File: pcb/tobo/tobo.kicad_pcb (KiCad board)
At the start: 2 copper layers, 57.5 x 61 mm, 87 parts, among them J2 Conn_01x02_Pin, J4 Molex 538-54548-2472, J5 Conn_01x09_Pin, J6 Conn_01x09_Pin, J7 Conn_01x09_Pin, J8 Hroparts Elec TYPE-C-31-M-12, U1 TS5A23167, U10 5015, U11 5015, U12 5015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

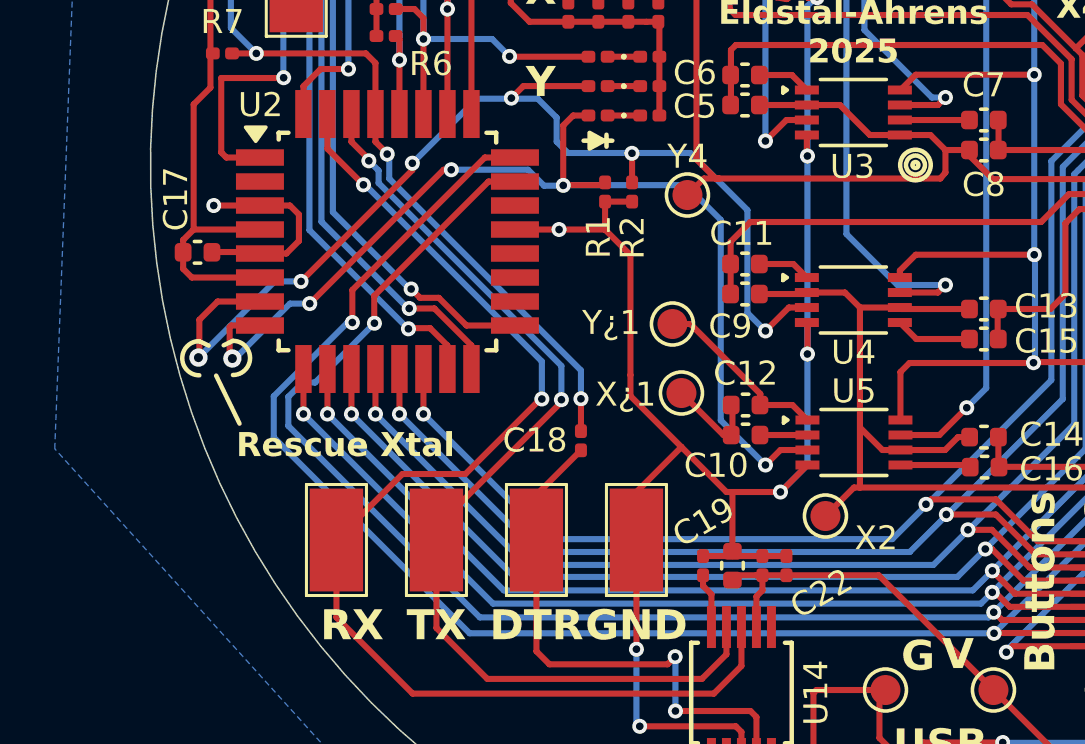
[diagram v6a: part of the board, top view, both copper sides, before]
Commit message: Solution to the PCB error in v0.3a
If you've got a v0.4 board, no need to futz around with RX/TX.
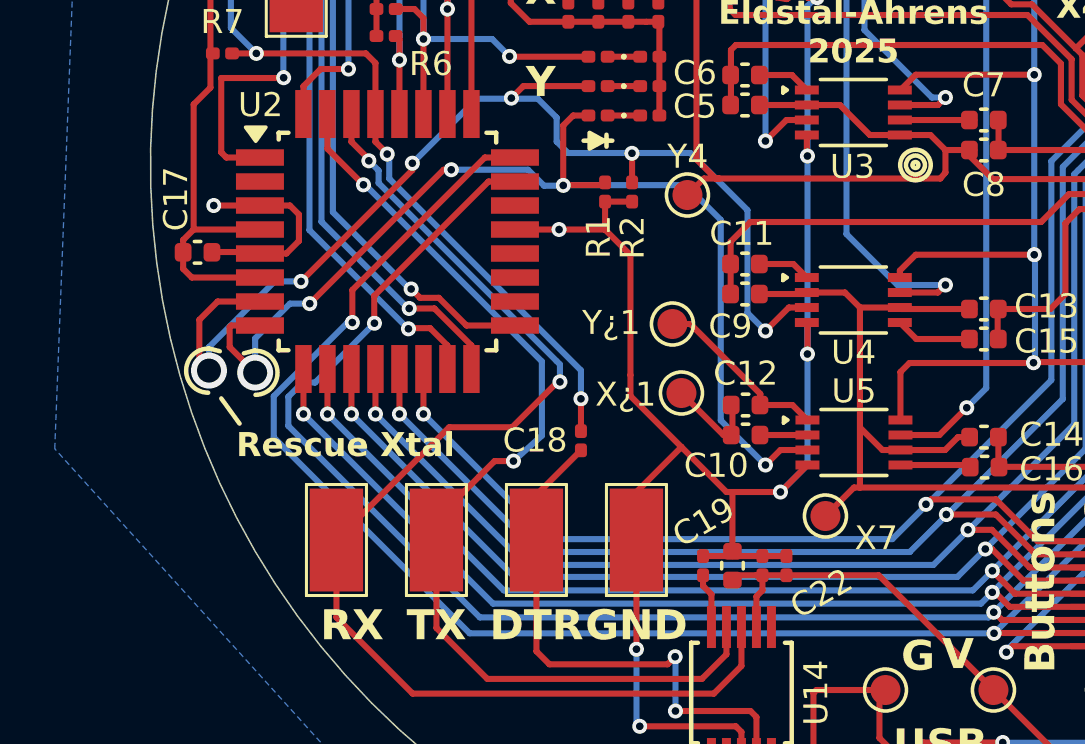
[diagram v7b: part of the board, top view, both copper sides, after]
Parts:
- J4: value Molex 538-54548-2472 -> 54548-2472
- U1, U3, U4, U5: value TS5A23167 -> TS5A23167DCUR
- renumbered X2 to X7
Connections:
- U2 pad 30: /TX -> /RX
- U2 pad 31: /RX -> /TX
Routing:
- net /2,6: track 37.3 -> 38.6 mm
- net /2,7: track 36.7 -> 37.4 mm

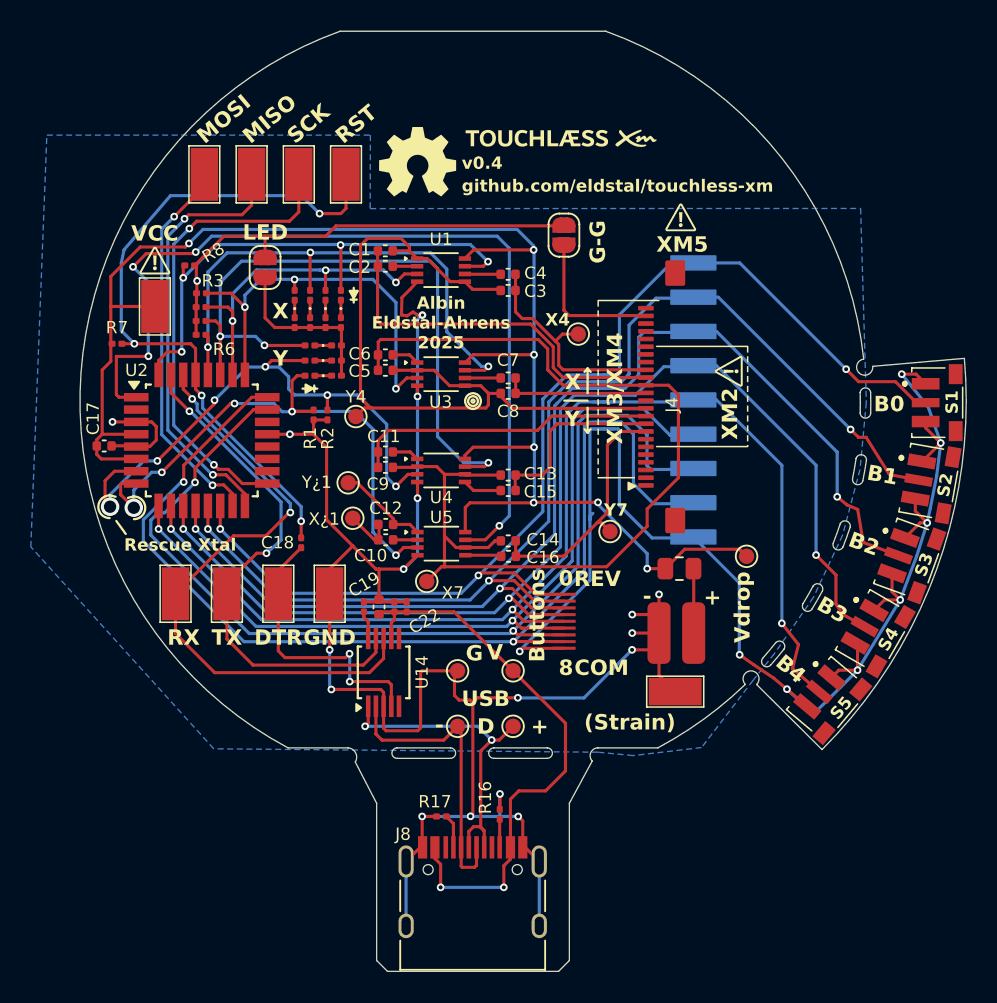
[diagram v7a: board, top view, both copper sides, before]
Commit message: PCB: Bump to Kicad 9 and preparation for step-up transformer
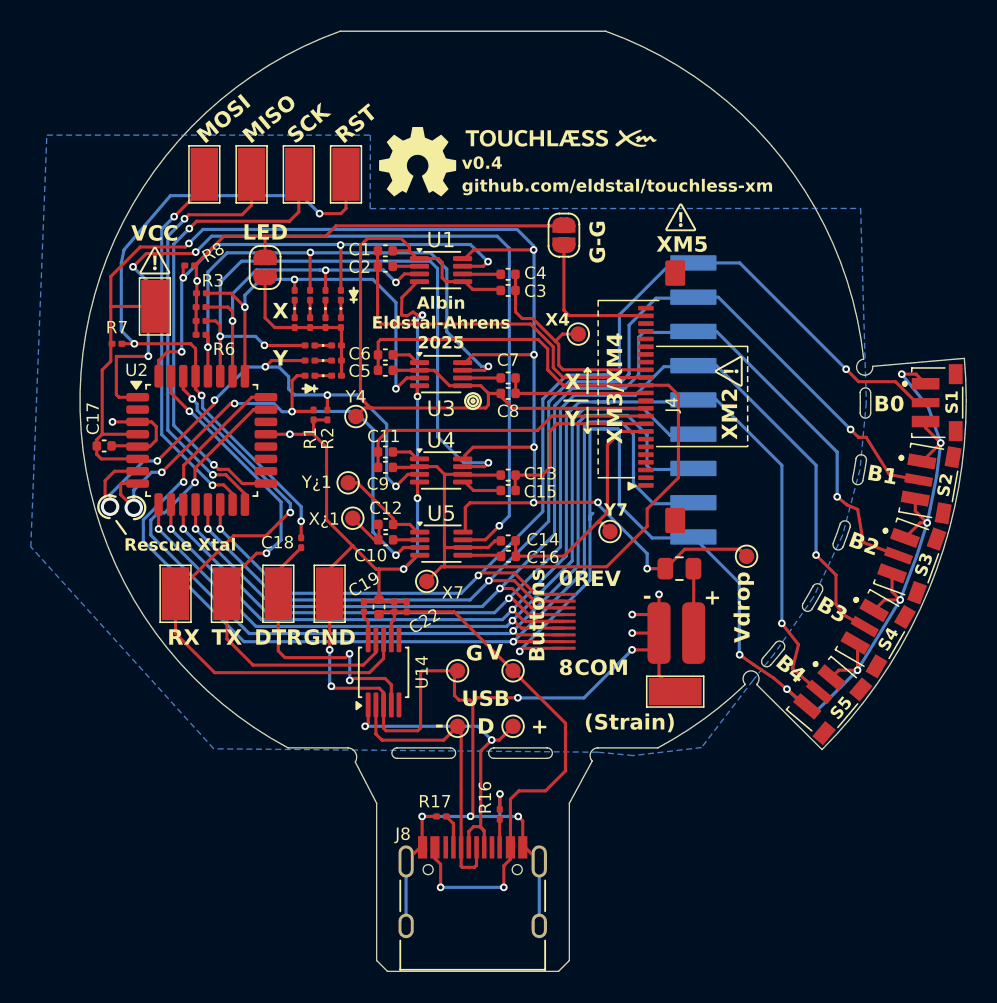
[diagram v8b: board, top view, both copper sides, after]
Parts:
- U1, U3, U4, U5: footprint Package_SO:VSSOP-8_2.3x2mm_P0.5mm -> tobo-footprints:VSSOP-8_2.3x2mm_P0.5mm_narrowpads
- U14: footprint Package_SO:MSOP-10_3x3mm_P0.5mm -> tobo-footprints:MSOP-10_3x3mm_P0.5mm_narrowpads
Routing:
- net /Y4: track 50.7 -> 51.6 mm
